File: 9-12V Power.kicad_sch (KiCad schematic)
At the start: 20 parts, among them U5 TPS54540BDDA, U6 MCP41HV51-104E/MQ

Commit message: updates to BOM and power connections
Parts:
- C-1, C-2, C-3, C-4: value 4.7u -> 4.7uF
- C-5: value 100n -> 0.1u; Digikey (none) -> 1276-1003-1-ND; LCSC (none) -> C1711; MPN (none) -> CL21B104KBCNNNC; Manufacturer (none) -> Samsung Electro-Mechanics
- L-1: value 10u -> 10uH
- U5: footprint (none) -> LEOS:SO-POWERPAD8_DDA_TEX; Digikey (none) -> 296-TPS54540BDDA-ND; MPN (none) -> TPS54540BDDA; Manufacturer (none) -> Texas Instruments
- U6: footprint (none) -> LEOS:QFN20_5x5MC_MCH; Digikey (none) -> MCP41HV51-104E/MQ-ND; MPN (none) -> MCP41HV51-104E/MQ; Manufacturer (none) -> Microchip Technology
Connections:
- net VIN: no longer C-1.1, C-2.1, C-3.1, C-4.1, R-1.1, U5.2 (VIN)
- net VDC: now reaches C-8.1, C-9.1, L-1.2, R-6.1
- new net VPP: C-1.1, C-2.1, C-3.1, C-4.1, R-1.1, U5.2 (VIN)

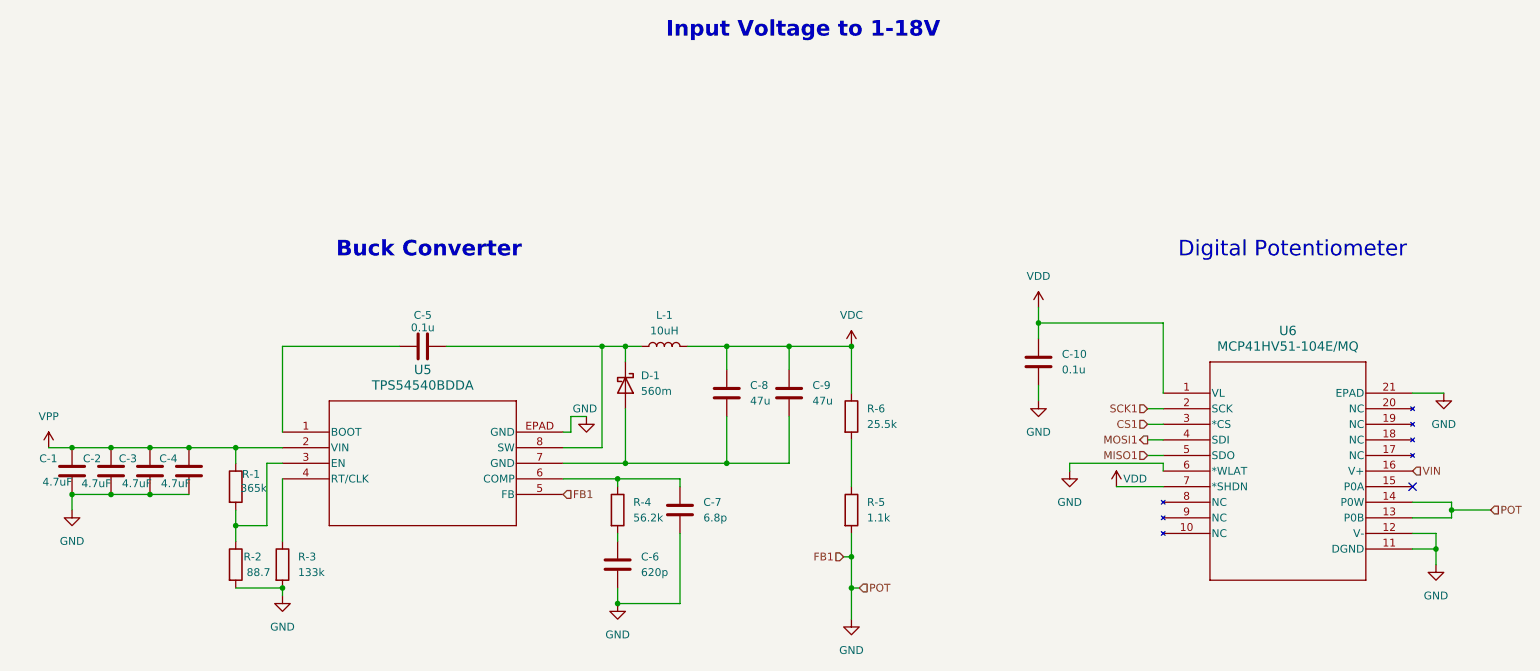
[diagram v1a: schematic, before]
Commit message: updates to BOM and fixes for ERC
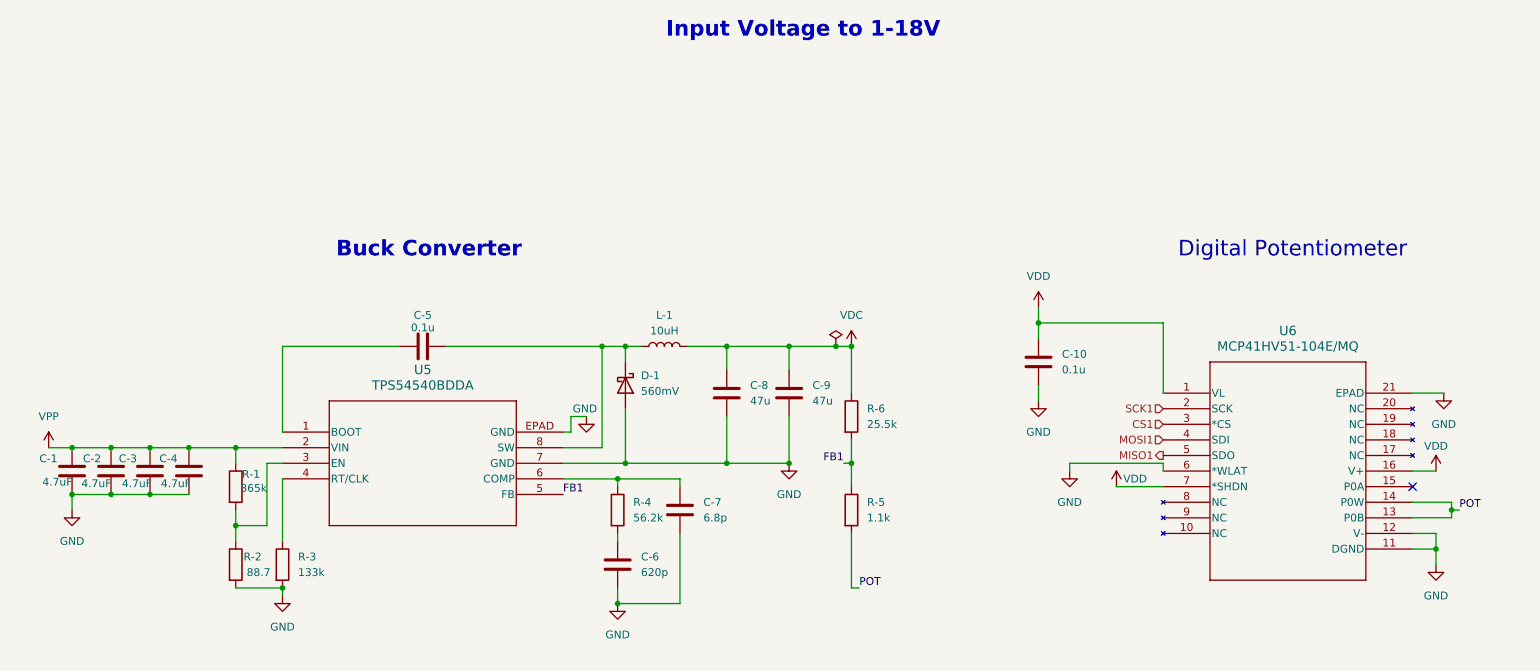
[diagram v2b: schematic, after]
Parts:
- C-8, C-9: footprint Capacitor_SMD:C_0805_2012Metric -> Capacitor_SMD:C_1206_3216Metric; Digikey (none) -> 4713-GMC31X5R476M25NTCT-ND; MPN (none) -> GMC31X5R476M25NT; Manufacturer (none) -> Cal-Chip Electronics, Inc.
- D-1: value 560m -> 560mV
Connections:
- net VIN is gone; now on net VDD: U6.16 (V+)
- net GND: now also C-8.2, C-9.2, D-1.2 (A), U5.7 (GND); no longer R-5.2, U5.5 (FB), U6.13 (P0B), U6.14 (P0W)
- net FB1: now reaches R-5.1, R-6.2
- net FB1: now also U5.5 (FB)
- new net POT: R-5.2, U6.13 (P0B), U6.14 (P0W)

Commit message: updates to BOM and beginning of routing
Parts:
- D-1: Digikey (none) -> VS-50WQ04FNHM3GI-ND; MPN (none) -> VS-50WQ04FNHM3; Manufacturer (none) -> Vishay General Semiconductor - Diodes Division
- L-1: footprint Inductor_SMD:L_0805_2012Metric -> LEOS:IND_TAIYO_NRS8030_TAY; Digikey (none) -> 587-2960-1-ND; MPN (none) -> NRS8030T100MJGJ; Manufacturer (none) -> Taiyo Yuden
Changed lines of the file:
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@@
 	(wire
 		(pts
+			(xy 240.03 85.09) (xy 245.11 85.09)
+		)
+		(stroke
+			(width 0)
+			(type default)
+		)
+	)
+	(wire
+		(pts
 			(xy 110.49 107.95) (xy 110.49 109.22)
 		)
@@
 	(wire
 		(pts
-			(xy 245.11 85.09) (xy 240.03 85.09)
-		)
-		(stroke
-			(width 0)
-			(type default)
-		)
-	)
-	(wire
-		(pts
 			(xy 246.38 102.87) (xy 246.38 104.14)
 		)
@@
 			)
 		)
-		(property "Footprint" "Inductor_SMD:L_0805_2012Metric"
+		(property "Footprint" "LEOS:IND_TAIYO_NRS8030_TAY"
 			(at 118.11 77.47 0)
 			(hide yes)
@@
 			)
 		)
+		(property "Digikey" "587-2960-1-ND"
+			(at 118.11 77.47 90)
+			(hide yes)
+			(show_name no)
+			(do_not_autoplace no)
+			(effects
+				(font
+					(size 1.27 1.27)
+				)
+			)
+		)
+		(property "MPN" "NRS8030T100MJGJ"
+			(at 118.11 77.47 90)
+			(hide yes)
+			(show_name no)
+			(do_not_autoplace no)
+			(effects
+				(font
+					(size 1.27 1.27)
+				)
+			)
+		)
+		(property "Manufacturer" "Taiyo Yuden"
+			(at 118.11 77.47 90)
+			(hide yes)
+			(show_name no)
+			(do_not_autoplace no)
+			(effects
+				(font
+					(size 1.27 1.27)
+				)
+			)
+		)
 		(pin "2"
 		)
@@
 			(hide yes)
 			(show_name no)
+			(do_not_autoplace no)
+			(effects
+				(font
+					(size 1.27 1.27)
+				)
+			)
+		)
+		(property "Digikey" "VS-50WQ04FNHM3GI-ND"
+			(at 111.76 83.82 90)
+			(hide yes)
+			(show_name no)
+			(do_not_autoplace no)
+			(effects
+				(font
+					(size 1.27 1.27)
+				)
+			)
+		)
+		(property "MPN" "VS-50WQ04FNHM3"
+			(at 111.76 83.82 90)
+			(hide yes)
+			(show_name no)
+			(do_not_autoplace no)
+			(effects
+				(font
+					(size 1.27 1.27)
+				)
+			)
+		)
+		(property "Manufacturer" "Vishay General Semiconductor - Diodes Division"
+			(at 111.76 83.82 90)
+			(hide yes)
+			(show_name no)

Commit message: updates to BOM
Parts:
- removed C-9: 47u, Capacitor_SMD:C_1206_3216Metric, symbol Device:C
- removed R-1: 365k, Resistor_SMD:R_0805_2012Metric, symbol Device:R
- removed R-2: 88.7, Resistor_SMD:R_0805_2012Metric, symbol Device:R
- added TPFB1-18: TestPoint, TestPoint:TestPoint_Loop_D2.60mm_Drill0.9mm_Beaded, symbol Connector:TestPoint
- C-8: footprint Capacitor_SMD:C_1206_3216Metric -> LEOS:CAPAE660X600N; Digikey 4713-GMC31X5R476M25NTCT-ND -> 399-A768EB476M1VLAE042CT-ND; MPN GMC31X5R476M25NT -> A768EB476M1VLAE042; Manufacturer Cal-Chip Electronics, Inc. -> KEMET
- D-1: value 560mV -> 60V 20A; footprint Diode_SMD:D_0805_2012Metric -> Diode_THT:D_DO-201AD_P15.24mm_Horizontal; Digikey VS-50WQ04FNHM3GI-ND -> 1655-SB2060CT-ND; MPN VS-50WQ04FNHM3 -> SB2060; Manufacturer Vishay General Semiconductor - Diodes Division -> SMC Diode Solutions
- L-1: footprint LEOS:IND_TAIYO_NRS8030_TAY -> LEOS:IND_BOURNS_SRR1280; Digikey 587-2960-1-ND -> SRR1280-100MCT-ND; MPN NRS8030T100MJGJ -> SRR1280-100M; Manufacturer Taiyo Yuden -> Bourns Inc.
- R-3: value 133k -> 390k; Digikey RMCF0805FT133KCT-ND -> RMCF0805FT390KCT-ND; MPN RMCF0805FT133K -> RMCF0805FT390K
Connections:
- net FB1: now also TPFB1-18.1
- no-connect marks 1 -> 2

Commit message: switching frequency
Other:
- note added: "Switching Frequency: 250kHz"
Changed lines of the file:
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@@
+		)
+	)
+	(text "Switching Frequency: 250kHz"
+		(exclude_from_sim no)
+		(at 71.882 117.602 0)
+		(effects
+			(font
+				(size 1.27 1.27)
+			)
 		)
 	)

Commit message: hid test points from bom
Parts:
- TPFB1-18: now left out of the parts list
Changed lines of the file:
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@@
 		(body_style 1)
 		(exclude_from_sim no)
-		(in_bom yes)
+		(in_bom no)
 		(on_board yes)
 		(in_pos_files yes)

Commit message: routing done
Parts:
- renumbered C-10 to C-9, R-3 to R-1, R-4 to R-2, R-5 to R-3, R-6 to R-4
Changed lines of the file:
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@@
 		(dnp no)
 		(fields_autoplaced yes)
-		(property "Reference" "R-3"
+		(property "Reference" "R-1"
 			(at 58.42 111.7599 0)
 			(show_name no)
@@
 			(project "LEOS-F26-power"
 				(path "/3703ddf2-8141-438d-86a8-1eaec9672d0d/64f3d4b9-893f-4f0f-938c-0da76e19fc55"
-					(reference "R-3")
+					(reference "R-1")
 					(unit 1)
 				)
@@
 		(dnp no)
 		(fields_autoplaced yes)
-		(property "Reference" "C-10"
+		(property "Reference" "C-9"
 			(at 182.88 78.7399 0)
 			(show_name no)
@@
 			(project "LEOS-F26-power"
 				(path "/3703ddf2-8141-438d-86a8-1eaec9672d0d/64f3d4b9-893f-4f0f-938c-0da76e19fc55"
-					(reference "C-10")
+					(reference "C-9")
 					(unit 1)
 				)
@@
 		(dnp no)
 		(fields_autoplaced yes)
-		(property "Reference" "R-4"
+		(property "Reference" "R-2"
 			(at 113.03 102.8699 0)
 			(show_name no)
@@
 			(project "LEOS-F26-power"
 				(path "/3703ddf2-8141-438d-86a8-1eaec9672d0d/64f3d4b9-893f-4f0f-938c-0da76e19fc55"
-					(reference "R-4")
+					(reference "R-2")
 					(unit 1)
 				)
@@
 		(dnp no)
 		(fields_autoplaced yes)
-		(property "Reference" "R-5"
+		(property "Reference" "R-3"
 			(at 151.13 102.8699 0)
 			(show_name no)
@@
 			(project "LEOS-F26-power"
 				(path "/3703ddf2-8141-438d-86a8-1eaec9672d0d/64f3d4b9-893f-4f0f-938c-0da76e19fc55"
-					(reference "R-5")
+					(reference "R-3")
 					(unit 1)
 				)
@@
 		(dnp no)
 		(fields_autoplaced yes)
-		(property "Reference" "R-6"
+		(property "Reference" "R-4"
 			(at 151.13 87.6299 0)
 			(show_name no)
@@
 			(project "LEOS-F26-power"
 				(path "/3703ddf2-8141-438d-86a8-1eaec9672d0d/64f3d4b9-893f-4f0f-938c-0da76e19fc55"
-					(reference "R-6")
+					(reference "R-4")
 					(unit 1)
 				)

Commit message: updates to BOM
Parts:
- C-1, C-2, C-3, C-4: Digikey 1276-2970-1-ND -> 1276-1248-1-ND; MPN CL21B475KOFNFNE -> CL21A475KBQNNNE
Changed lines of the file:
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@@
 			)
 		)
-		(property "Digikey" "1276-2970-1-ND"
+		(property "Digikey" "1276-1248-1-ND"
 			(at 27.94 97.79 0)
 			(hide yes)
@@
 			)
 		)
-		(property "MPN" "CL21B475KOFNFNE"
+		(property "MPN" "CL21A475KBQNNNE"
 			(at 27.94 97.79 0)
 			(hide yes)
@@
 			)
 		)
-		(property "Digikey" "1276-2970-1-ND"
+		(property "Digikey" "1276-1248-1-ND"
 			(at 21.59 97.79 0)
 			(hide yes)
@@
 			)
 		)
-		(property "MPN" "CL21B475KOFNFNE"
+		(property "MPN" "CL21A475KBQNNNE"
 			(at 21.59 97.79 0)
 			(hide yes)
@@
 			)
 		)
-		(property "Digikey" "1276-2970-1-ND"
+		(property "Digikey" "1276-1248-1-ND"
 			(at 40.64 97.79 0)
 			(hide yes)
@@
 			)
 		)
-		(property "MPN" "CL21B475KOFNFNE"
+		(property "MPN" "CL21A475KBQNNNE"
 			(at 40.64 97.79 0)
 			(hide yes)
@@
 			)
 		)
-		(property "Digikey" "1276-2970-1-ND"
+		(property "Digikey" "1276-1248-1-ND"
 			(at 34.29 97.79 0)
 			(hide yes)
@@
 			)
 		)
-		(property "MPN" "CL21B475KOFNFNE"
+		(property "MPN" "CL21A475KBQNNNE"
 			(at 34.29 97.79 0)
 			(hide yes)
